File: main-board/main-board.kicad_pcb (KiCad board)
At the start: 2 copper layers, 81.6 x 87.9 mm, 73 parts, among them J1 MOTOR0, J10 PROGRAMMER, J11 CAM0, J12 CAM1, J13 CAM2, J14 CAM3, J15 CAM4, J16 CAM5, J17 CAM6, J18 CAM7, J19 PowerBoard Interface, J2 MOTOR1, J20 IMU Breakout, J21 ICSP (DO NOT POPULATE), J3 MOTOR2, J4 MOTOR3, J5 RJ45, J6 MOTOR4, J7 MOTOR5, J8 MOTOR6, J9 MOTOR7, SW1 SW_SPST, T1 ATB2012E-50011M-T01, T2 ATB2012E-50011M-T01, U1 MCP2515-EST, U2 ATA6560, U3 ATmega2560-16AU | Main Proc, U4 MC14051B, U5 MC14051B, U6 SN75HVD3082EDR, U7 LTC1983ES6-5-TRPBF, U8 THS7314DR, U9 SN75HVD3082EDR, Y1 20MHz, Y2 20MHz

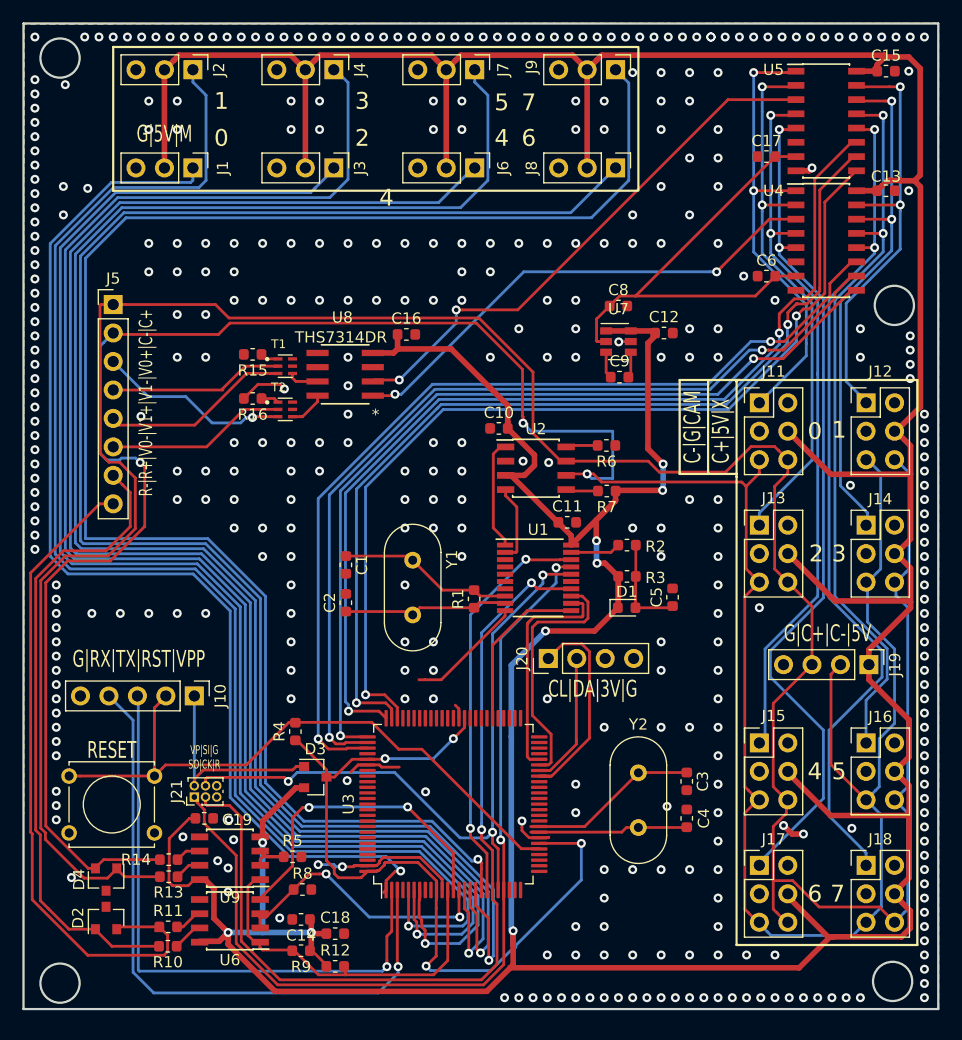
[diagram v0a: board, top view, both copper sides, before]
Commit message: S 1.0.1 B 1.0.1 change camera balancing to MAX4449ESE
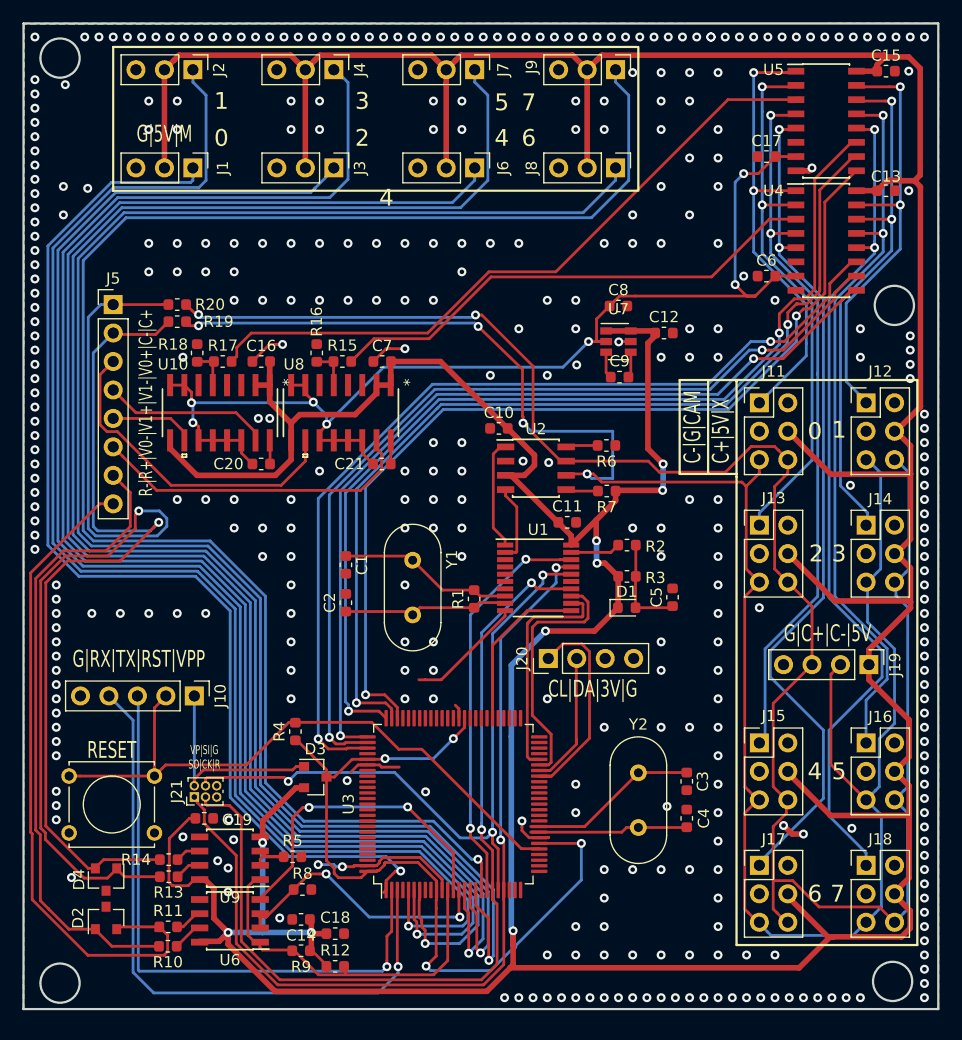
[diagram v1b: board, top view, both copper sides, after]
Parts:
- removed T1, T2: ATB2012E-50011M-T01, HHM1595A1:BALUN_HHM1595A1
- added C20: 100nF, Capacitor_SMD:C_0603_1608Metric, F.Cu at (86.2, 80.6)
- added C21: 100nF, Capacitor_SMD:C_0603_1608Metric, F.Cu at (97.0, 80.6)
- added C7: 100nF, Capacitor_SMD:C_0603_1608Metric, F.Cu at (97.0, 71.5)
- added R17: 75, Resistor_SMD:R_0603_1608Metric, F.Cu at (82.8, 71.5)
- added R18: 75, Resistor_SMD:R_0603_1608Metric, F.Cu at (80.5, 70.7)
- added R19: 0, Resistor_SMD:R_0603_1608Metric, F.Cu at (78.7, 67.9)
- added R20: 0, Resistor_SMD:R_0603_1608Metric, F.Cu at (78.7, 66.4)
- added U10: MAX4449ESE+, MAX4449ESE:MAX4449ESE&plus_, F.Cu at (82.5, 76.1)
- R15, R16: value 100 -> 75
- U8: value THS7314DR -> MAX4449ESE+; footprint ths7314dr:THS7314DR -> MAX4449ESE:MAX4449ESE&plus_
- moved C16 13.2 mm to (86.2, 71.5), turned to 180 degrees
- moved R15 8.03 mm to (93.5, 71.5), turned to 0 degrees
- moved R16 7.01 mm to (91.2, 70.7), turned to 270 degrees
- moved U8 3.45 mm to (93.3, 76.1), turned to 270 degrees
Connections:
- D4 pad 1: CAN+ -> RS485+2
- D4 pad 2: CAN- -> RS485-2
- J5 pad 1: CAN+ -> RS485+2
- J5 pad 2: CAN- -> RS485-2
- R13 pad 1: CAN+ -> RS485+2
- R14 pad 1: CAN- -> RS485-2
- R15 pad 2: GND -> VID-CAM0
- R16 pad 1: Net-(R16-Pad1) -> GND
- R16 pad 2: GND -> Net-(R15-Pad1)
- U8 pad 1: VID-CAM0 -> +5V
- U8 pad 2: VID-CAM1 -> +5V
- U8 pad 4: +5V -> Net-(U8-Pad4)
- U8 pad 5: GND -> Net-(R15-Pad1)
- U8 pad 7: Net-(T1-Pad4) -> -5V
- U8 pad 8: Net-(T2-Pad4) -> -5V
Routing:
- net RS485+2: track 0.00 -> 85.3 mm, vias 0 -> 1
- net RS485-2: track 0.00 -> 75.9 mm, vias 0 -> 1
- net CAN+: track 242.6 -> 167.7 mm, vias 0 -> 2
- net CAN-: track 255.1 -> 182.6 mm, vias 3 -> 4
- net -5V: track 42.1 -> 105.9 mm, vias 0 -> 7
- net +5V: track 544.7 -> 577.0 mm
- net VID0-: track 16.1 -> 29.7 mm
- net VID0+: track 17.2 -> 29.4 mm, vias 1 -> 0
- net VID-CAM1: track 49.3 -> 61.0 mm, vias 2 -> 0
- net VID1+: track 17.5 -> 7.58 mm
- net GND: track 45.5 -> 52.0 mm, vias 396 -> 379
- net Net-(R17-Pad1): track 0.00 -> 3.66 mm
- net Net-(T2-Pad4): track 3.32 -> 0.00 mm
- net Net-(T1-Pad4): track 2.76 -> 0.00 mm
- net Net-(R15-Pad1): track 1.63 -> 3.63 mm
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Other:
- board text added: "MISSOURI S&T UNDERWATER ROBOTICS TEAM MAIN BOARD | PCB 1.0.2 | SCH 1.0.2 MATTHEW (COOPER) HEALY, MICHAELA DICKERSON"
- board text removed: "MISSOURI S&T UNDERWATER ROBOTICS TEAM MAIN BOARD | PCB 1.0.1 | SCH 1.0.1 MATTHEW (COOPER) HEALY, MICHAELA DICKERSON"

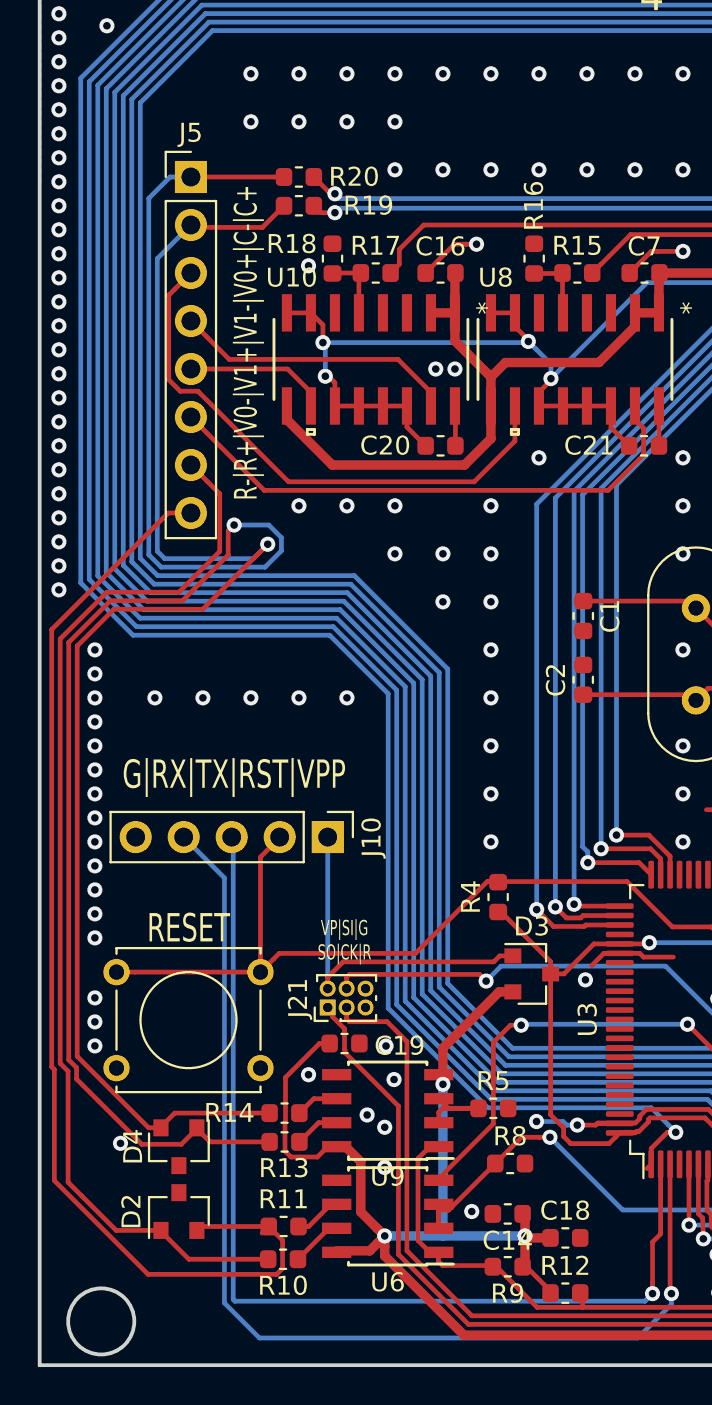
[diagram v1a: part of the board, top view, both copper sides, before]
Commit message: Removing old routes to support full duplex rs485
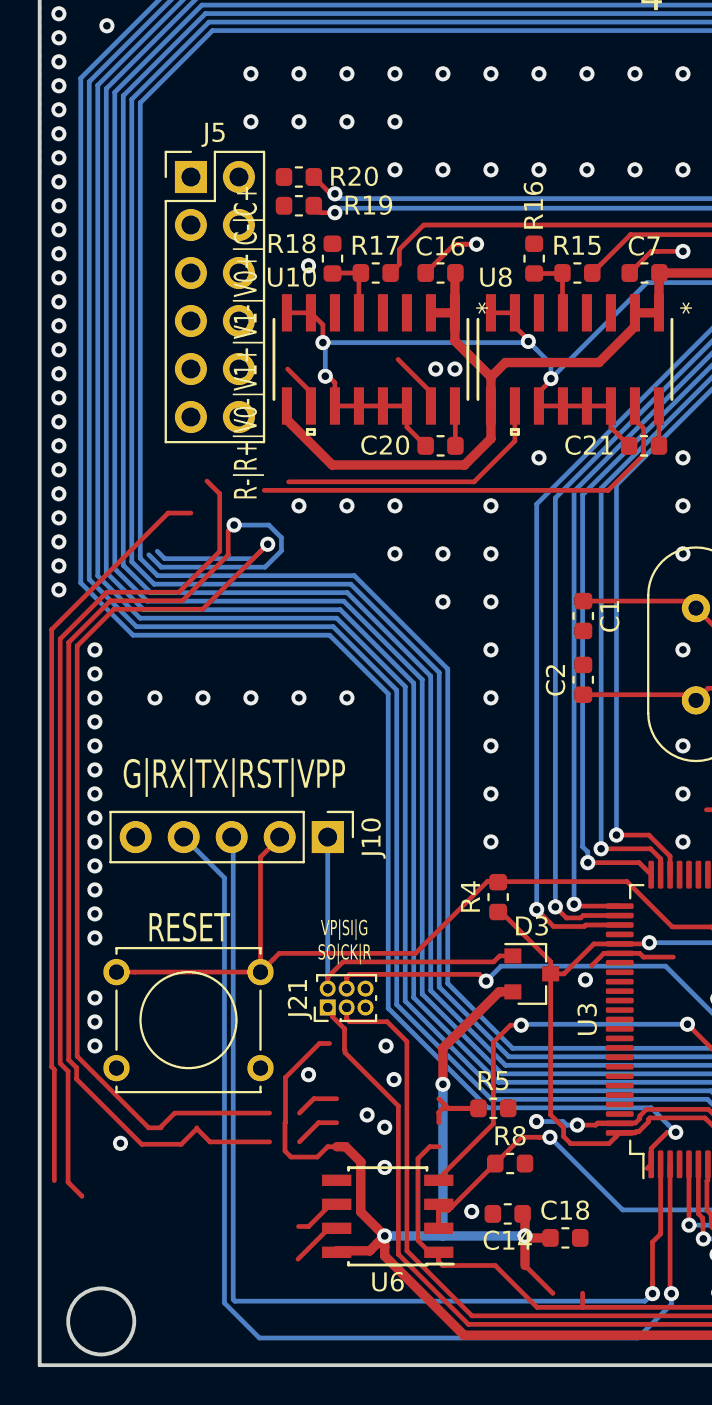
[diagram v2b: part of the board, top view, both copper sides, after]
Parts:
- removed C19: 100nF, Capacitor_SMD:C_0603_1608Metric
- removed D2, D4: CDSOT23-SM712, Package_TO_SOT_SMD:SOT-23
- removed R10, R11, R13, R14: 10, Resistor_SMD:R_0603_1608Metric
- removed R12, R9: 10k, Resistor_SMD:R_0603_1608Metric
- removed U9: SN75HVD3082EDR, Package_SO:SOIC-8_3.9x4.9mm_P1.27mm
- J5: value RJ45 -> Tether Interface; footprint Connector_PinHeader_2.54mm:PinHeader_1x08_P2.54mm_Vertical -> Connector_PinHeader_2.54mm:PinHeader_2x06_P2.54mm_Vertical
- R5, R8: value 10k -> 120
- U6: value SN75HVD3082EDR -> MAX490E
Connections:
- J5 pad 1: RS485+2 -> VID1-
- J5 pad 2: RS485-2 -> VID1+
- J5 pad 3: VID0+ -> VID0-
- J5 pad 4: VID1- -> VID0+
- J5 pad 5: VID1+ -> Net-(J5-Pad5)
- J5 pad 6: VID0- -> Net-(J5-Pad6)
- J5 pad 7: RS485+ -> Net-(J5-Pad7)
- J5 pad 8: RS485- -> Net-(J5-Pad8)
- R19 pad 2: RS485-2 -> Net-(J5-Pad8)
- R20 pad 2: RS485+2 -> Net-(J5-Pad7)
- R5 pad 1: Net-(R5-Pad1) -> CAN-
- R5 pad 2: GND -> CAN+
- R8 pad 1: RS485-DIR -> TX_L
- R8 pad 2: GND -> TX_H
- U3 pad 12: RS485-R -> R
- U3 pad 13: RS485-D -> D
- U3 pad 14: RS485-DIR -> Net-(U3-Pad14)
- U6 pad 1: RS485-R -> +5V
- U6 pad 2: RS485-DIR -> R
- U6 pad 3: RS485-DIR -> D
- U6 pad 4: RS485-D -> GND
- U6 pad 5: GND -> RX_H
- U6 pad 6: Net-(R11-Pad2) -> RX_L
- U6 pad 7: Net-(R10-Pad2) -> TX_L
- U6 pad 8: +5V -> TX_H
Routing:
- net RS485+2: track 85.3 -> 58.8 mm
- net RS485-2: track 75.9 -> 52.4 mm
- net RS485-: track 60.3 -> 39.1 mm
- net VID0+: track 29.4 -> 14.7 mm
- net RS485+: track 56.8 -> 44.3 mm
- net VID1-: track 15.0 -> 3.18 mm
- net VID0-: track 29.7 -> 24.4 mm
- net VID1+: track 7.58 -> 2.47 mm
- net Net-(R5-Pad1): track 5.05 -> 0.00 mm
- net CAN-: track 182.6 -> 187.7 mm
- net TX_L: track 0.00 -> 2.42 mm
- net Net-(R10-Pad2): track 2.42 -> 0.00 mm
- net RX_L: track 0.00 -> 2.31 mm
- net Net-(R11-Pad2): track 2.31 -> 0.00 mm

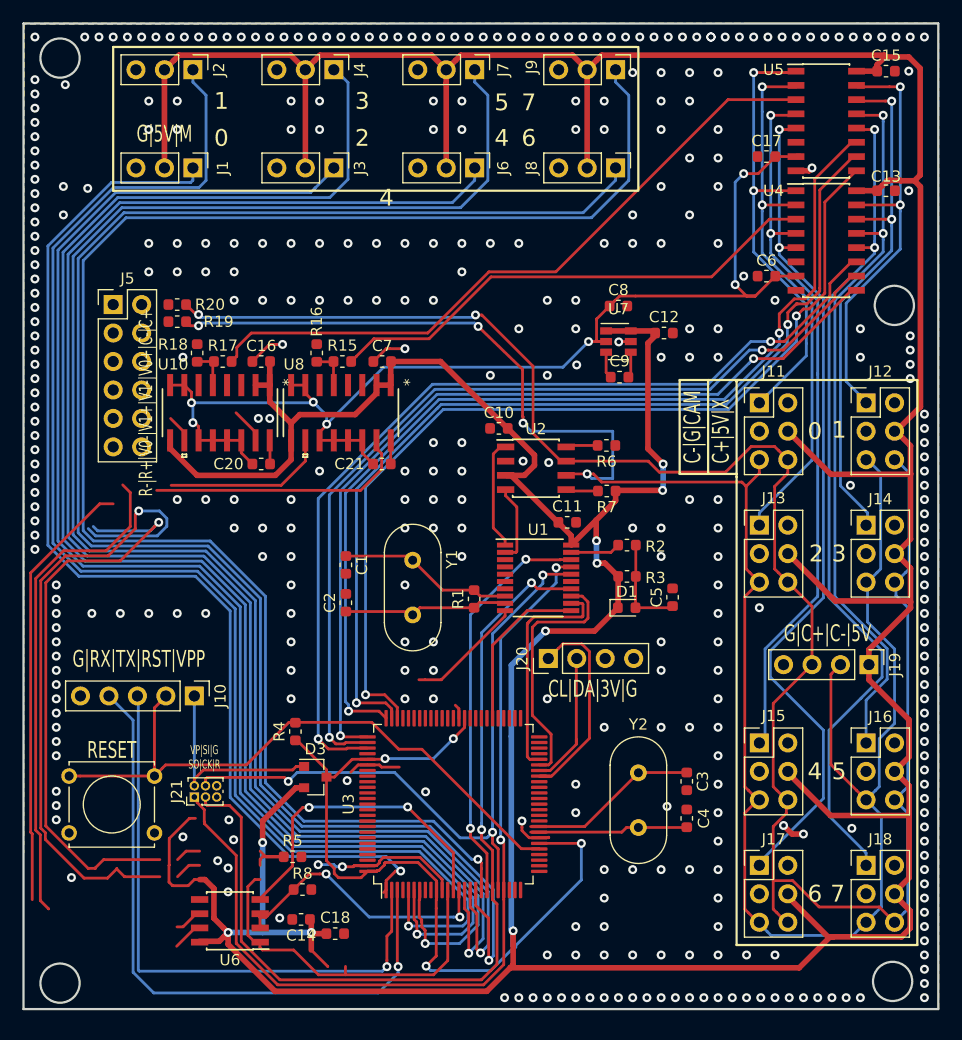
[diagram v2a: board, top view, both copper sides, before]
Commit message: S1.0.3 B1.0.3 See Desc
* various layout changes
* remove 0-ohm resistors on CAN
* add RS485 full-duplex
* add optional USB connection
* change crystal footprint
* I'm sure I've forgotten things sorry
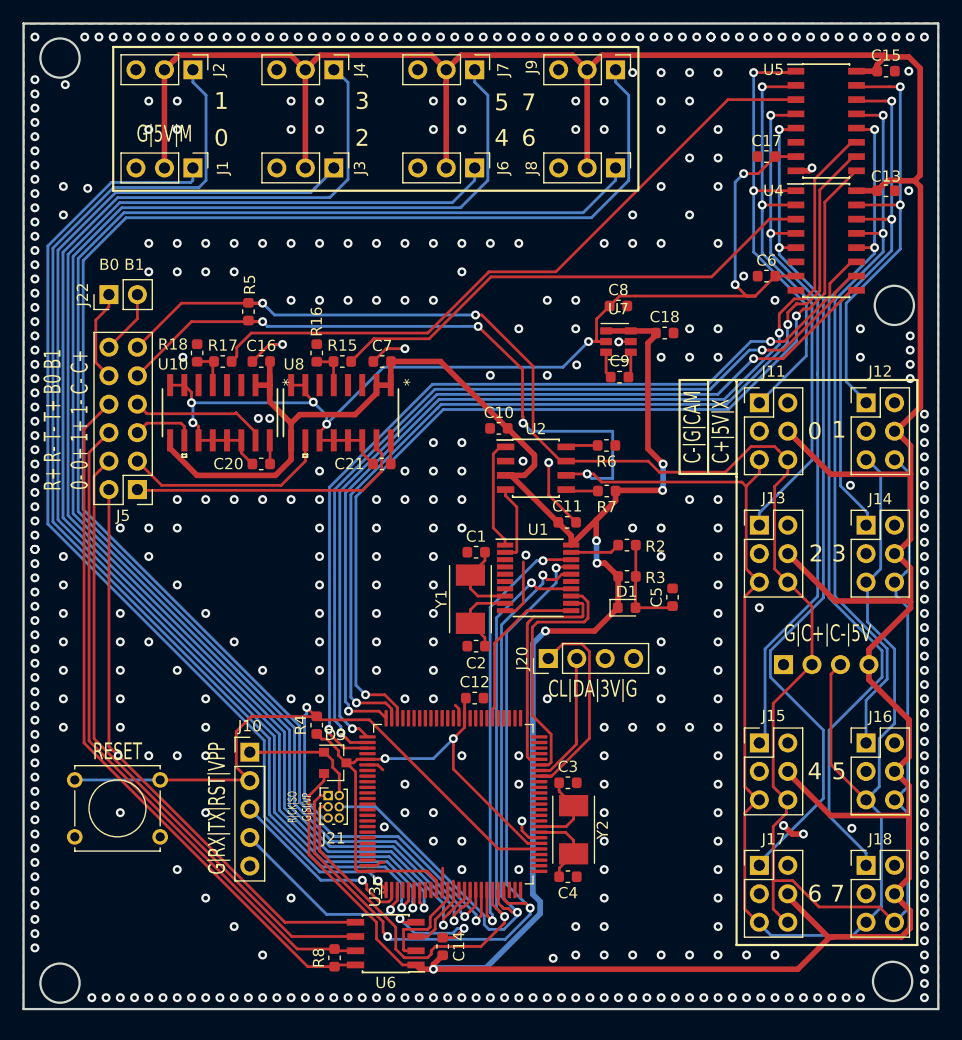
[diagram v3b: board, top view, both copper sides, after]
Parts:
- removed R1: 10k, Resistor_SMD:R_0603_1608Metric
- removed R19, R20: 0, Resistor_SMD:R_0603_1608Metric
- added J22: PLAN (US)B PINS, Connector_PinHeader_2.54mm:PinHeader_1x02_P2.54mm_Vertical, F.Cu at (72.6, 65.5)
- J19: footprint Connector_PinHeader_2.54mm:PinHeader_1x04_P2.54mm_Vertical -> Connector_PinSocket_2.54mm:PinSocket_1x04_P2.54mm_Vertical; moved to B.Cu
- J5: value Tether Interface -> TETHER INTERFACE
- Y1, Y2: footprint Crystal:Crystal_HC49-U_Vertical -> Crystal:Crystal_SMD_Abracon_ABM7-2Pin_6.0x3.5mm
- moved C18 61.1 mm to (122.2, 69.0)
- moved R5 48.8 mm to (85.1, 67.1), turned to 90 degrees
- moved C12 36.7 mm to (105.3, 101.5)
- moved J5 16.7 mm to (75.2, 82.9), turned to 180 degrees
- moved U6 14.1 mm to (97.3, 123.4)
- moved C14 12.9 mm to (102.4, 123.7), turned to 90 degrees
- moved C2 12.3 mm to (105.4, 96.9), turned to 180 degrees
- moved J21 11.9 mm to (92.2, 110.2), turned to 0 degrees
- moved C4 11.8 mm to (113.6, 117.5), turned to 0 degrees
- moved C1 11.7 mm to (105.4, 88.5), turned to 180 degrees
- moved C3 10.6 mm to (113.6, 109.1), turned to 0 degrees
- moved Y2 7.69 mm to (114.1, 113.3)
- moved J19 7.62 mm to (132.8, 98.6)
- moved J10 7.05 mm to (85.2, 106.4), turned to 0 degrees
- moved R8 6.73 mm to (92.8, 124.7), turned to 270 degrees
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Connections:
- C12 pad 1: +5V -> Net-(C12-Pad1)
- D3 pad 3: +5V -> Net-(C12-Pad1)
- J10 pad 2: RESET-MAIN -> RESET_MAIN
- J19 pad 1: +5V -> GND
- J19 pad 2: CAN- -> CAN+
- J19 pad 3: CAN+ -> CAN-
- J19 pad 4: GND -> +5V
- J5 pad 1: VID1- -> VID0-
- J5 pad 10: RX_H -> Net-(J22-Pad1)
- J5 pad 11: TX_L -> CAN+
- J5 pad 12: TX_H -> Net-(J22-Pad2)
- J5 pad 2: VID1+ -> RX_H
- J5 pad 3: VID0- -> VID0+
- J5 pad 4: VID0+ -> RX_L
- J5 pad 5: Net-(J5-Pad5) -> VID1+
- J5 pad 6: Net-(J5-Pad6) -> TX_L
- J5 pad 7: Net-(J5-Pad7) -> VID1-
- J5 pad 8: Net-(J5-Pad8) -> TX_H
- J5 pad 9: RX_L -> CAN-
- R4 pad 1: +5V -> Net-(C12-Pad1)
- R4 pad 2: RESET-MAIN -> RESET_MAIN
- SW1 pad 1: RESET-MAIN -> RESET_MAIN
- U3 pad 10: +5V -> Net-(C12-Pad1)
- U3 pad 100: +5V -> Net-(C12-Pad1)
- U3 pad 30: RESET-MAIN -> RESET_MAIN
- U3 pad 31: +5V -> Net-(C12-Pad1)
- U3 pad 61: +5V -> Net-(C12-Pad1)
- U3 pad 80: +5V -> Net-(C12-Pad1)
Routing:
- net +5V: track 577.0 -> 464.3 mm, vias 13 -> 6
- net RESET_MAIN: track 0.00 -> 65.3 mm, vias 0 -> 1
- net TX_H: track 0.00 -> 63.7 mm
- net RS485+2: track 58.8 -> 0.00 mm, vias 1 -> 0
- net TX_L: track 2.42 -> 59.8 mm
- net RESET-MAIN: track 56.2 -> 0.00 mm
- net RX_L: track 2.31 -> 56.0 mm
- net RS485-2: track 52.4 -> 0.00 mm, vias 1 -> 0
- net RX_H: track 0.48 -> 51.4 mm, vias 0 -> 1
- net Net-(C12-Pad1): track 0.00 -> 50.4 mm, vias 0 -> 2
- net RS485+: track 44.3 -> 0.00 mm
- net PROG0-RX: track 58.1 -> 17.6 mm
- net RS485-: track 39.1 -> 0.00 mm
- net PROG0-TX: track 53.9 -> 17.2 mm
- net RS485-R: track 33.0 -> 0.00 mm
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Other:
- board text added: "B0 B1"
- board text added: "MISSOURI S&T UNDERWATER ROBOTICS TEAM MAIN BOARD | PCB 1.0.3 | SCH 1.0.3 MATTHEW (COOPER) HEALY, MICHAELA DICKERSON"
- board text added: "R+ R- T- T+ B0 B1 0- 0+ 1+ 1- C- C+"
- board text added: "R|CK|SO G|SI|VP"
- board text removed: "MISSOURI S&T UNDERWATER ROBOTICS TEAM MAIN BOARD | PCB 1.0.2 | SCH 1.0.2 MATTHEW (COOPER) HEALY, MICHAELA DICKERSON"
- board text removed: "R-|R+|V0-|V1+|V1-|V0+|C-|C+"
- board text removed: "VP|SI|G SO|CK|R"
